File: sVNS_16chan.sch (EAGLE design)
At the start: 54 parts, among them IC1 EFM8SB10F8G-A-CSP16R, IC2 OPA990IDCKR, U1 NT3H2211W0FHKH, U2 LT8410EDC-1#TRMPBF, U3 MUX36S16IRSNR, U4 MUX36S16IRSNR

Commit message: Experimentation and routing
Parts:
- added J1: TSM-130-01-F-SV, TSM-130-01-F-SV:TSM-130-01-F-SV
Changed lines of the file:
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@@
 <part name="JP2" library="sVNS_16chan_lib" deviceset="PINHD-1X1" device="" package3d_urn="urn:adsk.eagle:package:22485/2"/>
 <part name="R21" library="sVNS_16chan_lib" deviceset="SMD_PADS" device="R0402" package3d_urn="urn:adsk.eagle:package:23547/3"/>
+<part name="J1" library="TSM-130-01-F-SV" deviceset="TSM-130-01-F-SV" device=""/>
 </parts>
 <sheets>
@@
 <attribute name="VALUE" x="128.27" y="83.058" size="1.778" layer="96"/>
 </instance>
+<instance part="J1" gate="G$1" x="68.58" y="-17.78" smashed="yes" rot="R270">
+<attribute name="NAME" x="107.796" y="-12.2" size="1.778" layer="95" rot="R270"/>
+<attribute name="VALUE" x="25.4" y="-12.7" size="1.778" layer="96" rot="R270"/>
+</instance>
 </instances>

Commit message: Replaced 0402 pads to 0603
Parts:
- R12, R14, R15, R16, R17, R18, R19, R20, R21, R22, R23, R24, R25: device sVNS_16chan_lib:SMD_PADSR0402 -> sVNS_16chan_lib:SMD_PADS_0603
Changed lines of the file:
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@@
 <part name="DEBUG_N_2510_SOCKET" library="N2510-6002RB" deviceset="N2510-6002RB" device=""/>
 <part name="C14" library="rcl" library_urn="urn:adsk.eagle:library:334" deviceset="C-EU" device="C0402" package3d_urn="urn:adsk.eagle:package:23626/2" value="0.1 uF"/>
-<part name="R12" library="sVNS_16chan_lib" deviceset="SMD_PADS" device="R0402" package3d_urn="urn:adsk.eagle:package:23547/3"/>
-<part name="R14" library="sVNS_16chan_lib" deviceset="SMD_PADS" device="R0402" package3d_urn="urn:adsk.eagle:package:23547/3"/>
-<part name="R15" library="sVNS_16chan_lib" deviceset="SMD_PADS" device="R0402" package3d_urn="urn:adsk.eagle:package:23547/3"/>
-<part name="R16" library="sVNS_16chan_lib" deviceset="SMD_PADS" device="R0402" package3d_urn="urn:adsk.eagle:package:23547/3"/>
-<part name="R17" library="sVNS_16chan_lib" deviceset="SMD_PADS" device="R0402" package3d_urn="urn:adsk.eagle:package:23547/3"/>
-<part name="R18" library="sVNS_16chan_lib" deviceset="SMD_PADS" device="R0402" package3d_urn="urn:adsk.eagle:package:23547/3"/>
-<part name="R19" library="sVNS_16chan_lib" deviceset="SMD_PADS" device="R0402" package3d_urn="urn:adsk.eagle:package:23547/3"/>
-<part name="R20" library="sVNS_16chan_lib" deviceset="SMD_PADS" device="R0402" package3d_urn="urn:adsk.eagle:package:23547/3"/>
-<part name="R22" library="sVNS_16chan_lib" deviceset="SMD_PADS" device="R0402" package3d_urn="urn:adsk.eagle:package:23547/3"/>
-<part name="R23" library="sVNS_16chan_lib" deviceset="SMD_PADS" device="R0402" package3d_urn="urn:adsk.eagle:package:23547/3"/>
-<part name="R24" library="sVNS_16chan_lib" deviceset="SMD_PADS" device="R0402" package3d_urn="urn:adsk.eagle:package:23547/3"/>
-<part name="R25" library="sVNS_16chan_lib" deviceset="SMD_PADS" device="R0402" package3d_urn="urn:adsk.eagle:package:23547/3"/>
+<part name="R12" library="sVNS_16chan_lib" deviceset="SMD_PADS_0603" device="" package3d_urn="urn:adsk.eagle:package:23555/3"/>
+<part name="R14" library="sVNS_16chan_lib" deviceset="SMD_PADS_0603" device="" package3d_urn="urn:adsk.eagle:package:23555/3"/>
+<part name="R15" library="sVNS_16chan_lib" deviceset="SMD_PADS_0603" device="" package3d_urn="urn:adsk.eagle:package:23555/3"/>
+<part name="R16" library="sVNS_16chan_lib" deviceset="SMD_PADS_0603" device="" package3d_urn="urn:adsk.eagle:package:23555/3"/>
+<part name="R17" library="sVNS_16chan_lib" deviceset="SMD_PADS_0603" device="" package3d_urn="urn:adsk.eagle:package:23555/3"/>
+<part name="R18" library="sVNS_16chan_lib" deviceset="SMD_PADS_0603" device="" package3d_urn="urn:adsk.eagle:package:23555/3"/>
+<part name="R19" library="sVNS_16chan_lib" deviceset="SMD_PADS_0603" device="" package3d_urn="urn:adsk.eagle:package:23555/3"/>
+<part name="R20" library="sVNS_16chan_lib" deviceset="SMD_PADS_0603" device="" package3d_urn="urn:adsk.eagle:package:23555/3"/>
+<part name="R22" library="sVNS_16chan_lib" deviceset="SMD_PADS_0603" device="" package3d_urn="urn:adsk.eagle:package:23555/3"/>
+<part name="R23" library="sVNS_16chan_lib" deviceset="SMD_PADS_0603" device="" package3d_urn="urn:adsk.eagle:package:23555/3"/>
+<part name="R24" library="sVNS_16chan_lib" deviceset="SMD_PADS_0603" device="" package3d_urn="urn:adsk.eagle:package:23555/3"/>
+<part name="R25" library="sVNS_16chan_lib" deviceset="SMD_PADS_0603" device="" package3d_urn="urn:adsk.eagle:package:23555/3"/>
 <part name="JP1" library="sVNS_16chan_lib" deviceset="PINHD-1X1" device="" package3d_urn="urn:adsk.eagle:package:22485/2"/>
 <part name="JP2" library="sVNS_16chan_lib" deviceset="PINHD-1X1" device="" package3d_urn="urn:adsk.eagle:package:22485/2"/>
-<part name="R21" library="sVNS_16chan_lib" deviceset="SMD_PADS" device="R0402" package3d_urn="urn:adsk.eagle:package:23547/3"/>
+<part name="R21" library="sVNS_16chan_lib" deviceset="SMD_PADS_0603" device="" package3d_urn="urn:adsk.eagle:package:23555/3"/>
 <part name="J1" library="TSM-130-01-F-SV" deviceset="TSM-130-01-F-SV" device=""/>
 </parts>

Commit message: 1) Updated .gitignore as per online recommendations 2)  sch: added third sheet, separated output stage     sch: deleted old pin     sch: added surface mount male connectors and preliminary routed them 3)  brd: draft component location. MUXes and pads on bottom.     Op amp and LT8410 on bottom. H bridge, NT3H and EFM8 on top.     Ready for experiments. GND plane created. No pwr plane yet.
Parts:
- removed ANTENNA: Antenna connector, pinhead:PINHD-1X2
- added J2, J3: M50-3631042, M50-3631042:M50-3631042
- J1: value TSM-130-01-F-SV -> M50-3631042; device TSM-130-01-F-SV:TSM-130-01-F-SV -> M50-3631042:M50-3631042
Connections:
- net S10A: now also J1.10
- net S10B: now also J3.10
- net S11A: now also J2.1
- net S11B: now also J2.5
- net S12A: now also J2.2
- net S12B: now also J2.6
- net S13A: now also J2.3
- net S13B: now also J2.7
- net S14A: now also J2.4
- net S14B: now also J2.8
- net S1A: now also J1.1
- net S1B: now also J3.1
- net S2A: now also J1.2
- net S2B: now also J3.2
- net S3A: now also J1.3
- net S3B: now also J3.3
- net S4A: now also J1.4
- net S4B: now also J3.4
- net S5A: now also J1.5
- net S5B: now also J3.5
- net S6A: now also J1.6
- net S6B: now also J3.6
- net S7A: now also J1.7
- net S7B: now also J3.7
- net S8A: now also J1.8
- net S8B: now also J3.8
- net S9A: now also J1.9
- net S9B: now also J3.9

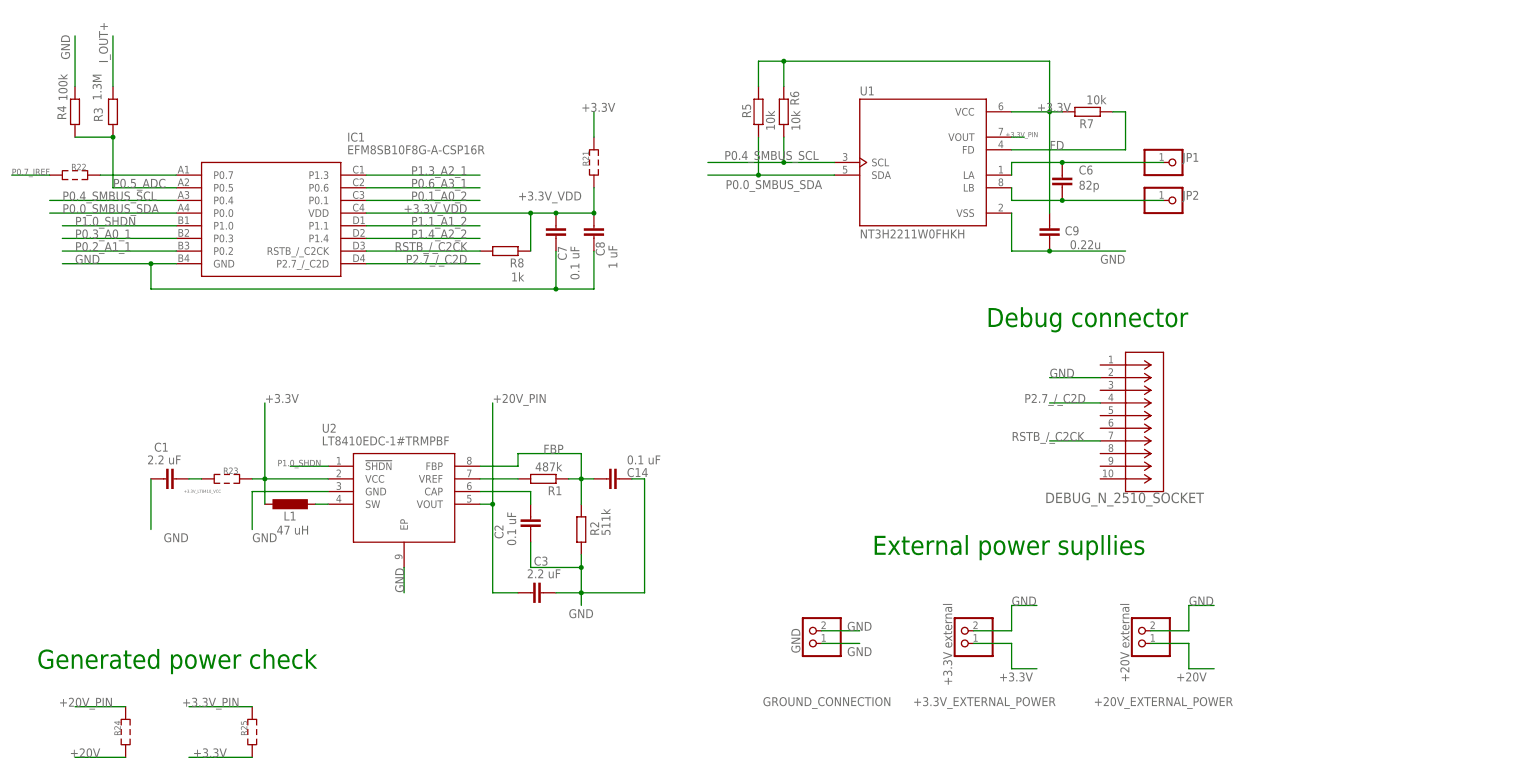
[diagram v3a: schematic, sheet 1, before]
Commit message: Changed MCU package from CSP to QFN20. Ready to route signal traces. Ready for MUXS16 rotations
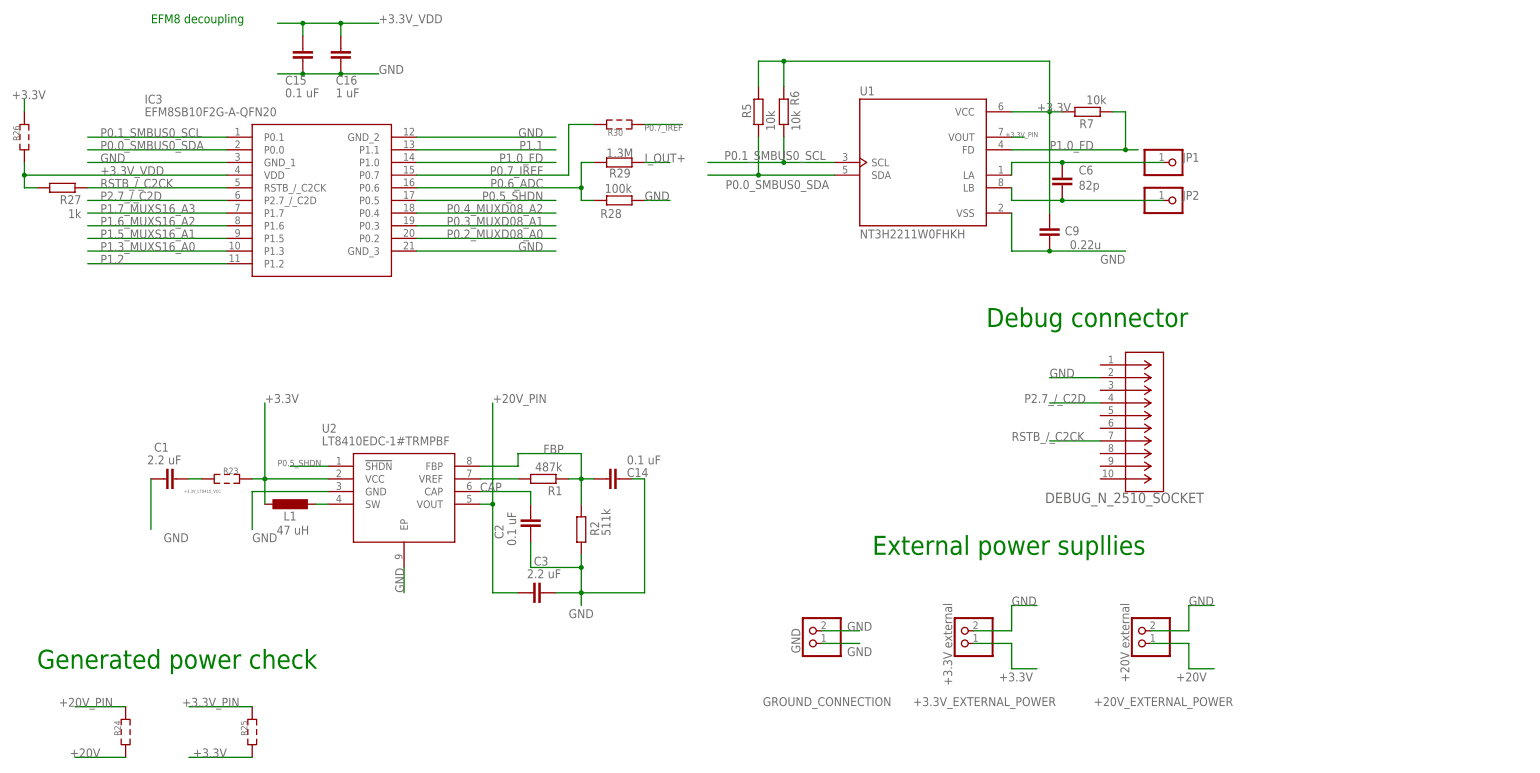
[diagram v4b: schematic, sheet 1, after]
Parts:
- removed C7: 0.1 uF, rcl:C-EUC0402
- removed C8: 1 uF, rcl:C-EUC0402
- removed IC1: EFM8SB10F8G-A-CSP16R, sVNScomponents:EFM8SB10F8G-A-CSP16R
- removed R21, R22: (no value), sVNS_16chan_lib:SMD_PADS_0603
- removed R3: 1.3M, rcl:R-EU_R0402
- removed R4: 100k, rcl:R-EU_R0402
- removed R8: 1k, rcl:R-EU_R0402
- added C15: 0.1 uF, rcl:C-EUC0402
- added C16: 1 uF, rcl:C-EUC0402
- added IC3: EFM8SB10F2G-A-QFN20, SamacSys_Parts:EFM8SB10F2G-A-QFN20
- added R26, R30: (no value), sVNS_16chan_lib:SMD_PADS_0603
- added R27: 1k, rcl:R-EU_R0402
- added R28: 100k, rcl:R-EU_R0402
- added R29: 1.3M, rcl:R-EU_R0402
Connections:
- net N$58 renamed CAP
- removed net FD: R7.1, U1.FD
- removed net P0.0_SMBUS_SDA: IC1.P0.0, R5.1, U1.SDA
- removed net P0.1_A0_2: IC1.P0.1, U$1.A0
- removed net P0.2_A1_1: IC1.P0.2, U3.A1, U4.A1
- removed net P0.3_A0_1: IC1.P0.3, U3.A0, U4.A0
- removed net P0.4_SMBUS_SCL: IC1.P0.4, R6.1, U1.SCL
- removed net P0.5_ADC: IC1.P0.5, R3.1, R4.2
- removed net P0.6_A3_1: IC1.P0.6, U3.A3, U4.A3
- removed net P0.7_IREF_PIN: IC1.P0.7, R22.2
- removed net P1.0_SHDN: IC1.P1.0, U$1.EN, U2.!SHDN, U3.EN, U4.EN
- removed net P1.1_A1_2: IC1.P1.1, U$1.A1
- removed net P1.3_A2_1: IC1.P1.3, U3.A2, U4.A2
- removed net P1.4_A2_2: IC1.P1.4, U$1.A2
- new net P0.0_SMBUS0_SDA: IC3.P0.0, R5.1, U1.SDA
- new net P0.1_SMBUS0_SCL: IC3.P0.1, R6.1, U1.SCL
- new net P0.2_MUXD08_A0: IC3.P0.2, U$1.A0
- new net P0.3_MUXD08_A1: IC3.P0.3, U$1.A1
- new net P0.4_MUXD08_A2: IC3.P0.4, U$1.A2
- new net P0.5_SHDN: IC3.P0.5, U$1.EN, U2.!SHDN, U3.EN, U4.EN
- new net P0.6_ADC: IC3.P0.6, R28.1, R29.2
- new net P1.0_FD: IC3.P1.0, R7.1, U1.FD
- new net P1.1: IC3.P1.1
- new net P1.2: IC3.P1.2
- new net P1.3_MUXS16_A0: IC3.P1.3, U3.A0, U4.A0
- new net P1.5_MUXS16_A1: IC3.P1.5, U3.A1, U4.A1
- new net P1.6_MUXS16_A2: IC3.P1.6, U3.A2, U4.A2
- new net P1.7_MUXS16_A3: IC3.P1.7, U3.A3, U4.A3
- net +3.3V: now also R26.2; no longer R21.2
- net +3.3V_VDD: now also C15.2, C16.1, IC3.VDD, R26.1, R27.2; no longer C7.2, C8.1, IC1.VDD, R21.1, R8.1
- net GND: now also C15.1, C16.2, IC3.GND_1, IC3.GND_2, IC3.GND_3, R28.2; no longer C7.1, C8.2, IC1.GND, R4.1
- net I_OUT+: now also R29.1; no longer R3.2
- net P0.7_IREF: now also IC3.P0.7, R30.1, R30.2; no longer R22.1
- net P2.7_/_C2D: now also IC3.P2.7_/_C2D; no longer IC1.P2.7_/_C2D
- net RSTB_/_C2CK: now also IC3.RSTB_/_C2CK, R27.1; no longer IC1.RSTB_/_C2CK, R8.2
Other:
- note added: "EFM8 decoupling"

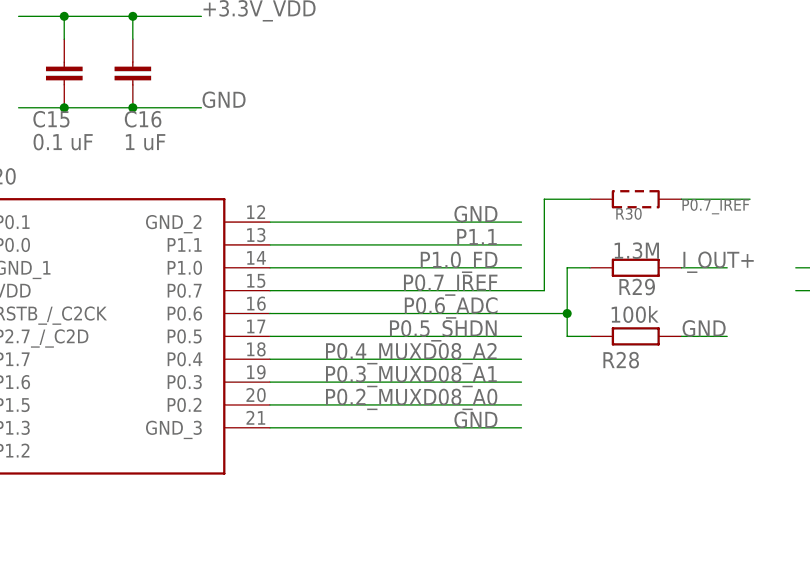
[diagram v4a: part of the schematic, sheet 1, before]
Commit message: Optimized component placement. Ready for signal routing. Ready for power/gnd vias.
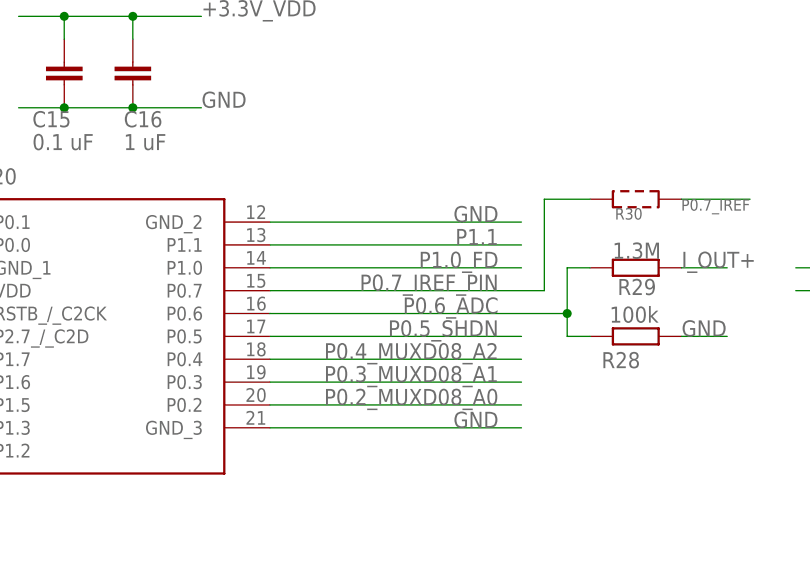
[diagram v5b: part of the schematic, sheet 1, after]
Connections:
- new net P0.7_IREF_PIN: IC3.P0.7, R30.2
- net P0.7_IREF: no longer IC3.P0.7, R30.2
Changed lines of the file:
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@@
 <net name="P0.7_IREF" class="0">
-<segment>
-<pinref part="IC3" gate="G$1" pin="P0.7"/>
-<wire x1="88.9" y1="134.62" x2="119.38" y2="134.62" width="0.1524" layer="91"/>
-<label x="114.3" y="134.62" size="1.778" layer="95" align="bottom-right"/>
-<wire x1="119.38" y1="134.62" x2="119.38" y2="144.78" width="0.1524" layer="91"/>
-<pinref part="R30" gate="G$1" pin="2"/>
-<wire x1="119.38" y1="144.78" x2="124.46" y2="144.78" width="0.1524" layer="91"/>
-</segment>
 <segment>
 <wire x1="134.62" y1="144.78" x2="142.24" y2="144.78" width="0.1524" layer="91"/>
@@
 </segment>
 </net>
+<net name="P0.7_IREF_PIN" class="0">
+<segment>
+<pinref part="IC3" gate="G$1" pin="P0.7"/>
+<wire x1="88.9" y1="134.62" x2="119.38" y2="134.62" width="0.1524" layer="91"/>
+<label x="114.3" y="134.62" size="1.778" layer="95" align="bottom-right"/>
+<wire x1="119.38" y1="134.62" x2="119.38" y2="144.78" width="0.1524" layer="91"/>
+<pinref part="R30" gate="G$1" pin="2"/>
+<wire x1="119.38" y1="144.78" x2="124.46" y2="144.78" width="0.1524" layer="91"/>
+</segment>
+</net>
